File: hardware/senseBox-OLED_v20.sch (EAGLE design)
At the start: 25 parts, among them IC2 VREG-TS9011-3V3, J1 JUMPER2-0402-NC, J2 JST4-B4B-PH-SM4-TB, T3 BSS138PS, X1 PASSER-07, X2 PASSER-07, X3 PASSER-07, X4 PASSER-07

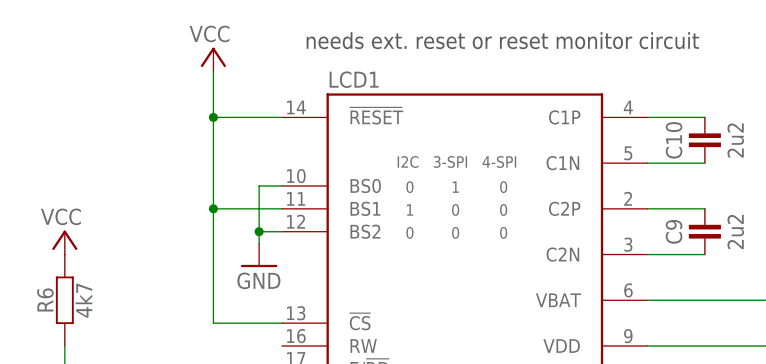
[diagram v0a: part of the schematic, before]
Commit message: updated schematics
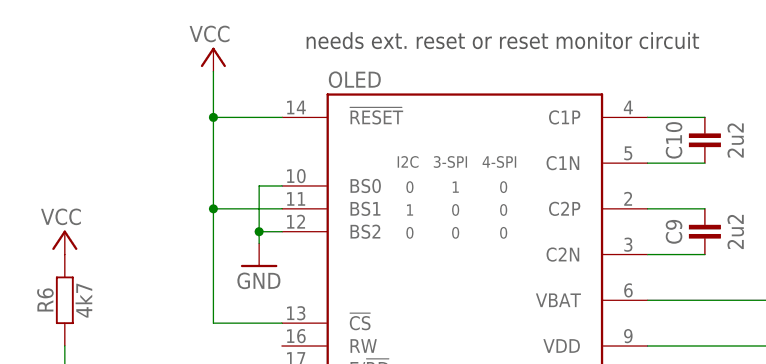
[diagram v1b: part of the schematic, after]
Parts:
- renumbered LCD1 to OLED
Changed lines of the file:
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@@
 <setting verticaltext="up"/>
 </settings>
-<grid distance="0.05" unitdist="inch" unit="inch" style="lines" multiple="1" display="yes" altdistance="0.025" altunitdist="inch" altunit="inch"/>
+<grid distance="0.1" unitdist="inch" unit="inch" style="lines" multiple="1" display="no" altdistance="0.01" altunitdist="inch" altunit="inch"/>
 <layers>
 <layer number="1" name="Top" color="4" fill="1" visible="no" active="no"/>
@@
 <part name="C4" library="we-rcl" deviceset="CAPACITOR" device="-0402" value="100n"/>
 <part name="C1" library="we-rcl" deviceset="CAPACITOR" device="-0402" value="100n"/>
-<part name="LCD1" library="we-opto" deviceset="UG2864HSWEG01" device="-B"/>
+<part name="OLED" library="we-opto" deviceset="UG2864HSWEG01" device="-B"/>
 <part name="P+7" library="supply1" deviceset="VCC" device=""/>
 <part name="GND7" library="supply1" deviceset="GND" device=""/>
@@
 <instance part="C4" gate="C" x="139.7" y="21.59" rot="R90"/>
 <instance part="C1" gate="C" x="86.36" y="21.59" rot="R90"/>
-<instance part="LCD1" gate="LCD" x="113.03" y="114.3"/>
+<instance part="OLED" gate="LCD" x="113.03" y="114.3"/>
 <instance part="P+7" gate="VCC" x="85.09" y="147.32" smashed="yes">
 <attribute name="VALUE" x="86.995" y="149.86" size="1.778" layer="96" rot="R180"/>
@@
 </segment>
 <segment>
-<pinref part="LCD1" gate="LCD" pin="BS2"/>
+<pinref part="OLED" gate="LCD" pin="BS2"/>
 <wire x1="92.71" y1="127" x2="90.17" y2="127" width="0.1524" layer="91"/>
 <wire x1="92.71" y1="132.08" x2="90.17" y2="132.08" width="0.1524" layer="91"/>
@@
 <wire x1="90.17" y1="127" x2="90.17" y2="125.73" width="0.1524" layer="91"/>
 <junction x="90.17" y="127"/>
-<pinref part="LCD1" gate="LCD" pin="BS0"/>
+<pinref part="OLED" gate="LCD" pin="BS0"/>
 </segment>
 <segment>
@@
 </segment>
 <segment>
-<pinref part="LCD1" gate="LCD" pin="AGND"/>
-<pinref part="LCD1" gate="LCD" pin="GND@3"/>
+<pinref part="OLED" gate="LCD" pin="AGND"/>
+<pinref part="OLED" gate="LCD" pin="GND@3"/>
 <wire x1="133.35" y1="86.36" x2="133.35" y2="88.9" width="0.1524" layer="91"/>
-<pinref part="LCD1" gate="LCD" pin="GND@2"/>
+<pinref part="OLED" gate="LCD" pin="GND@2"/>
 <wire x1="133.35" y1="88.9" x2="133.35" y2="91.44" width="0.1524" layer="91"/>
 <junction x="133.35" y="88.9"/>
-<pinref part="LCD1" gate="LCD" pin="GND@1"/>
+<pinref part="OLED" gate="LCD" pin="GND@1"/>
 <wire x1="133.35" y1="91.44" x2="133.35" y2="93.98" width="0.1524" layer="91"/>
 <junction x="133.35" y="91.44"/>
@@
 </segment>
 <segment>
-<pinref part="LCD1" gate="LCD" pin="!RESET"/>
+<pinref part="OLED" gate="LCD" pin="!RESET"/>
 <pinref part="P+7" gate="VCC" pin="VCC"/>
 <wire x1="92.71" y1="139.7" x2="85.09" y2="139.7" width="0.1524" layer="91"/>
 <wire x1="85.09" y1="139.7" x2="85.09" y2="144.78" width="0.1524" layer="91"/>
-<pinref part="LCD1" gate="LCD" pin="!CS"/>
+<pinref part="OLED" gate="LCD" pin="!CS"/>
 <wire x1="92.71" y1="116.84" x2="85.09" y2="116.84" width="0.1524" layer="91"/>
 <wire x1="85.09" y1="116.84" x2="85.09" y2="129.54" width="0.1524" layer="91"/>
 <junction x="85.09" y="139.7"/>
-<pinref part="LCD1" gate="LCD" pin="BS1"/>
+<pinref part="OLED" gate="LCD" pin="BS1"/>
 <wire x1="85.09" y1="129.54" x2="85.09" y2="139.7" width="0.1524" layer="91"/>
 <wire x1="92.71" y1="129.54" x2="85.09" y2="129.54" width="0.1524" layer="91"/>
@@
 </segment>
 <segment>
-<pinref part="LCD1" gate="LCD" pin="VBAT"/>
+<pinref part="OLED" gate="LCD" pin="VBAT"/>
 <pinref part="P+2" gate="VCC" pin="VCC"/>
 <wire x1="133.35" y1="119.38" x2="158.75" y2="119.38" width="0.1524" layer="91"/>
@@
 <wire x1="165.1" y1="100.33" x2="165.1" y2="119.38" width="0.1524" layer="91"/>
 <junction x="165.1" y="119.38"/>
-<pinref part="LCD1" gate="LCD" pin="VDD"/>
+<pinref part="OLED" gate="LCD" pin="VDD"/>
 <pinref part="C7" gate="C" pin="2"/>
 <wire x1="133.35" y1="114.3" x2="158.75" y2="114.3" width="0.1524" layer="91"/>
@@
 <wire x1="90.17" y1="101.6" x2="85.09" y2="101.6" width="0.1524" layer="91"/>
 <label x="85.09" y="101.6" size="1.27" layer="95" rot="R180" xref="yes"/>
-<pinref part="LCD1" gate="LCD" pin="D2/SDA"/>
+<pinref part="OLED" gate="LCD" pin="D2/SDA"/>
 <wire x1="92.71" y1="99.06" x2="90.17" y2="99.06" width="0.1524" layer="91"/>
 <wire x1="90.17" y1="99.06" x2="90.17" y2="101.6" width="0.1524" layer="91"/>
-<pinref part="LCD1" gate="LCD" pin="D1/DIN/SDA"/>
+<pinref part="OLED" gate="LCD" pin="D1/DIN/SDA"/>
 <wire x1="90.17" y1="101.6" x2="92.71" y2="101.6" width="0.1524" layer="91"/>
 <junction x="90.17" y="101.6"/>
@@
 <wire x1="92.71" y1="104.14" x2="85.09" y2="104.14" width="0.1524" layer="91"/>
 <label x="85.09" y="104.14" size="1.27" layer="95" rot="R180" xref="yes"/>
-<pinref part="LCD1" gate="LCD" pin="D0/SCK"/>
+<pinref part="OLED" gate="LCD" pin="D0/SCK"/>
 </segment>
 </net>
 <net name="SA0" class="0">
 <segment>
-<pinref part="LCD1" gate="LCD" pin="DC/I2C_SA0"/>
+<pinref part="OLED" gate="LCD" pin="DC/I2C_SA0"/>
 <wire x1="92.71" y1="109.22" x2="68.58" y2="109.22" width="0.1524" layer="91"/>
 <wire x1="68.58" y1="109.22" x2="68.58" y2="114.3" width="0.1524" layer="91"/>
@@
 <net name="C2N" class="0">
 <segment>
-<pinref part="LCD1" gate="LCD" pin="C2N"/>
+<pinref part="OLED" gate="LCD" pin="C2N"/>
 <wire x1="133.35" y1="124.46" x2="139.7" y2="124.46" width="0.1524" layer="91"/>
 <pinref part="C9" gate="C" pin="1"/>
@@
 <net name="C2P" class="0">
 <segment>
-<pinref part="LCD1" gate="LCD" pin="C2P"/>
+<pinref part="OLED" gate="LCD" pin="C2P"/>
 <wire x1="133.35" y1="129.54" x2="139.7" y2="129.54" width="0.1524" layer="91"/>
 <pinref part="C9" gate="C" pin="2"/>
@@
 <net name="C1N" class="0">
 <segment>
-<pinref part="LCD1" gate="LCD" pin="C1N"/>
+<pinref part="OLED" gate="LCD" pin="C1N"/>
 <wire x1="133.35" y1="134.62" x2="139.7" y2="134.62" width="0.1524" layer="91"/>
 <pinref part="C10" gate="C" pin="1"/>
@@
 <net name="C1P" class="0">
 <segment>
-<pinref part="LCD1" gate="LCD" pin="C1P"/>
+<pinref part="OLED" gate="LCD" pin="C1P"/>
 <wire x1="133.35" y1="139.7" x2="139.7" y2="139.7" width="0.1524" layer="91"/>
 <pinref part="C10" gate="C" pin="2"/>
@@
 <net name="IREF" class="0">
 <segment>
-<pinref part="LCD1" gate="LCD" pin="IREF"/>
+<pinref part="OLED" gate="LCD" pin="IREF"/>
 <pinref part="R5" gate="R" pin="1"/>
 <wire x1="138.43" y1="99.06" x2="133.35" y2="99.06" width="0.1524" layer="91"/>
@@
 <net name="VCH" class="0">
 <segment>
-<pinref part="LCD1" gate="LCD" pin="VCOMH"/>
+<pinref part="OLED" gate="LCD" pin="VCOMH"/>
 <pinref part="C5" gate="C" pin="2"/>
 <wire x1="133.35" y1="104.14" x2="146.05" y2="104.14" width="0.1524" layer="91"/>
@@
 <net name="VC" class="0">
 <segment>
-<pinref part="LCD1" gate="LCD" pin="VCC"/>
+<pinref part="OLED" gate="LCD" pin="VCC"/>
 <pinref part="C6" gate="C" pin="2"/>
 <wire x1="133.35" y1="109.22" x2="152.4" y2="109.22" width="0.1524" layer="91"/>
